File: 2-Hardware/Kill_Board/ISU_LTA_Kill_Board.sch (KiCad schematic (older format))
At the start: 31 parts, among them P1 CONN_01X02, P10 CONN_2, P12 CONN_2, P14 CONN_2, P16 CONN_2, P18 CONN_2, P2 CONN_01X02, P3 CONN_01X02, P4 CONN_01X03, P5 CONN_01X03, P6 CONN_01X03, P8 CONN_2, Q1 NMOS+PMOS, Q2 N-CH, Q3 N-CH, U1 ADAFRUIT_FEATHER, U2 LM2937

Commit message: Getting ready for fab
Unable to make board.  Footprint for Feather is lost, started working on new footprint but not complete yet.
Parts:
- removed R?: R_Shunt_US, symbol Device:R_Shunt_US
- C1, C2: footprint (none) -> Capacitors_SMD:C_0805_HandSoldering
- P1, P2, P3: footprint Connectors_Ian:CONN_2.54mm_1x2 -> Pin_Headers:Pin_Header_Angled_1x02_Pitch2.54mm
- P10: renamed from P14; footprint Connectors:DEANS_MICRO -> Connectors_JST:JST_VH_B2P-VH-B_2x3.96mm_Vertical
- P11: renamed from P16; footprint Connectors:DEANS_MICRO -> Connectors_JST:JST_VH_B2P-VH-B_2x3.96mm_Vertical
- P12: renamed from P18; footprint Connectors:DEANS_MICRO -> Connectors_JST:JST_VH_B2P-VH-B_2x3.96mm_Vertical
- P4, P5, P6: footprint Connectors_Ian:CONN_2.54mm_1x3 -> Pin_Headers:Pin_Header_Angled_1x03_Pitch2.54mm
- P7: renamed from P8; footprint Connectors:DEANS_MICRO -> Connectors_JST:JST_VH_B2P-VH-B_2x3.96mm_Vertical
- P8: renamed from P10; footprint Connectors:DEANS_MICRO -> Connectors_JST:JST_VH_B2P-VH-B_2x3.96mm_Vertical
- P9: renamed from P12; footprint Connectors:DEANS_MICRO -> Connectors_JST:JST_VH_B2P-VH-B_2x3.96mm_Vertical
- Q1: footprint SMD:SOT-23-6 -> TO_SOT_Packages_SMD:SOT-23-6
- R2: renamed from R1; footprint (none) -> Resistors_SMD:R_0805_HandSoldering
- R3: renamed from R2; footprint (none) -> Resistors_SMD:R_0805_HandSoldering
- R4: renamed from R3; footprint (none) -> Resistors_SMD:R_0805_HandSoldering
- R5: renamed from R4; footprint (none) -> Resistors_SMD:R_0805_HandSoldering
- R6: renamed from R5; footprint (none) -> Resistors_SMD:R_0805_HandSoldering
- R7: renamed from R6; footprint (none) -> Resistors_SMD:R_0805_HandSoldering
- R8: renamed from R7; footprint (none) -> Resistors_SMD:R_0805_HandSoldering
- R9: renamed from R8; footprint (none) -> Resistors_SMD:R_0805_HandSoldering
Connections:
- wire segments 118 -> 114
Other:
- moved on the sheet: P1

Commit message: Got correct footprint for feather, placed all parts on board
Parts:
- BT1: footprint Wire_Pads:SolderWirePad_2x_1-5mmDrill -> Connector_Wire:SolderWirePad_1x02_P7.62mm_Drill2.5mm
- D1: footprint LEDs:LED_0805 -> LED_SMD:LED_0805_2012Metric_Pad1.15x1.40mm_HandSolder
- Q1: footprint TO_SOT_Packages_SMD:SOT-23-6 -> Package_TO_SOT_SMD:SOT-23-6_Handsoldering
- Q2, Q3: footprint TO_SOT_Packages_SMD:SOT-404 -> Package_TO_SOT_SMD:TO-263-3_TabPin2
- S1: footprint Switches:DPDT_ESWITCH_EG2207 -> Button_Switch_THT:SW_CuK_JS202011CQN_DPDT_Straight
- U1: footprint Modules_Ian:ADAFRUIT_FEATHER -> Adafruit:AdafruitFeather
- U2: footprint TO_SOT_Packages_SMD:SOT-223 -> Package_TO_SOT_SMD:SOT-223
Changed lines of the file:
@@
 F 0 "Q1" H 5100 5090 60  0000 R CNN
 F 1 "NMOS+PMOS" H 5100 4720 60  0000 R CNN
-F 2 "TO_SOT_Packages_SMD:SOT-23-6" H 5100 4900 60  0001 C CNN
+F 2 "Package_TO_SOT_SMD:SOT-23-6_Handsoldering" H 5100 4900 60  0001 C CNN
 F 3 "" H 5100 4900 60  0001 C CNN
 F 4 "FDC6333CCT-ND" H 5100 4900 60  0001 C CNN "DigikeyNumber"
@@
 F 0 "Q1" H 5100 4490 60  0000 R CNN
 F 1 "NMOS+PMOS" H 5100 4120 60  0000 R CNN
-F 2 "TO_SOT_Packages_SMD:SOT-23-6" H 5100 4300 60  0001 C CNN
+F 2 "Package_TO_SOT_SMD:SOT-23-6_Handsoldering" H 5100 4300 60  0001 C CNN
 F 3 "" H 5100 4300 60  0001 C CNN
 F 4 "FDC6333CCT-ND" H 5100 4300 60  0001 C CNN "DigikeyNumber"
@@
 F 0 "Q2" H 6210 5270 60  0000 R CNN
 F 1 "N-CH" H 6210 4950 60  0000 R CNN
-F 2 "TO_SOT_Packages_SMD:SOT-404" H 6200 5100 60  0001 C CNN
+F 2 "Package_TO_SOT_SMD:TO-263-3_TabPin2" H 6200 5100 60  0001 C CNN
 F 3 "" H 6200 5100 60  0001 C CNN
 F 4 "568-6587-1-ND" H 6200 5100 60  0001 C CNN "DigikeyNumber"
@@
 F 0 "Q3" H 6210 6220 60  0000 R CNN
 F 1 "N-CH" H 6210 5900 60  0000 R CNN
-F 2 "TO_SOT_Packages_SMD:SOT-404" H 6200 6050 60  0001 C CNN
+F 2 "Package_TO_SOT_SMD:TO-263-3_TabPin2" H 6200 6050 60  0001 C CNN
 F 3 "" H 6200 6050 60  0001 C CNN
 F 4 "568-6587-1-ND" H 6200 6050 60  0001 C CNN "DigikeyNumber"
@@
 F 0 "U2" H 3700 4254 60  0000 C CNN
 F 1 "LM2937" H 3550 4650 60  0000 C CNN
-F 2 "TO_SOT_Packages_SMD:SOT-223" H 3550 4450 60  0001 C CNN
+F 2 "Package_TO_SOT_SMD:SOT-223" H 3550 4450 60  0001 C CNN
 F 3 "" H 3550 4450 60  0001 C CNN
 F 4 "LM2937IMP-3.3/NOPBCT-ND" H 3550 4450 60  0001 C CNN "DigikeyNumber"
@@
 F 0 "S1" H 5600 4750 60  0000 C CNN
 F 1 "DPDT" H 5500 5000 60  0000 C CNN
-F 2 "Switches:DPDT_ESWITCH_EG2207" H 5500 4850 60  0001 C CNN
+F 2 "Button_Switch_THT:SW_CuK_JS202011CQN_DPDT_Straight" H 5500 4850 60  0001 C CNN
 F 3 "" H 5500 4850 60  0001 C CNN
 F 4 "EG1940-ND" H 5500 4850 60  0001 C CNN "DigikeyNumber"
@@
 F 0 "S1" H 3600 3900 60  0000 C CNN
 F 1 "DPDT" H 3500 4150 60  0000 C CNN
-F 2 "Switches:DPDT_ESWITCH_EG2207" H 3500 4000 60  0001 C CNN
+F 2 "Button_Switch_THT:SW_CuK_JS202011CQN_DPDT_Straight" H 3500 4000 60  0001 C CNN
 F 3 "" H 3500 4000 60  0001 C CNN
 F 4 "EG1940-ND" H 3500 4000 60  0001 C CNN "DigikeyNumber"
@@
 F 0 "D1" H 7050 4750 50  0000 C CNN
 F 1 "LED" H 7050 4550 50  0000 C CNN
-F 2 "LEDs:LED_0805" H 7050 4650 60  0001 C CNN
+F 2 "LED_SMD:LED_0805_2012Metric_Pad1.15x1.40mm_HandSolder" H 7050 4650 60  0001 C CNN
 F 3 "" H 7050 4650 60  0001 C CNN
 F 4 "754-1141-1-ND" H 7050 4650 60  0001 C CNN "DigikeyNumber"
@@
 F 0 "BT1" H 2000 4800 50  0000 C CNN
 F 1 "BATTERY" H 2000 4410 50  0000 C CNN
-F 2 "Wire_Pads:SolderWirePad_2x_1-5mmDrill" H 2000 4600 60  0001 C CNN
+F 2 "Connector_Wire:SolderWirePad_1x02_P7.62mm_Drill2.5mm" H 2000 4600 60  0001 C CNN
 F 3 "" H 2000 4600 60  0001 C CNN
 	1    2000 4600
@@
 F 0 "U1" V 2350 1200 60  0000 C CNN
 F 1 "ADAFRUIT_FEATHER" V 2350 2000 60  0000 C CNN
-F 2 "Modules_Ian:ADAFRUIT_FEATHER" H 2300 1550 60  0001 C CNN
+F 2 "Adafruit:AdafruitFeather" H 2300 1550 60  0001 C CNN
 F 3 "" H 2300 1550 60  0000 C CNN
 	1    2150 1750
@@
 F 0 "U1" V 3450 1200 60  0000 C CNN
 F 1 "ADAFRUIT_FEATHER" V 3450 2000 60  0000 C CNN
-F 2 "Modules_Ian:ADAFRUIT_FEATHER" H 3400 1550 60  0001 C CNN
+F 2 "Adafruit:AdafruitFeather" H 3400 1550 60  0001 C CNN
 F 3 "" H 3400 1550 60  0000 C CNN
 	2    3250 1750

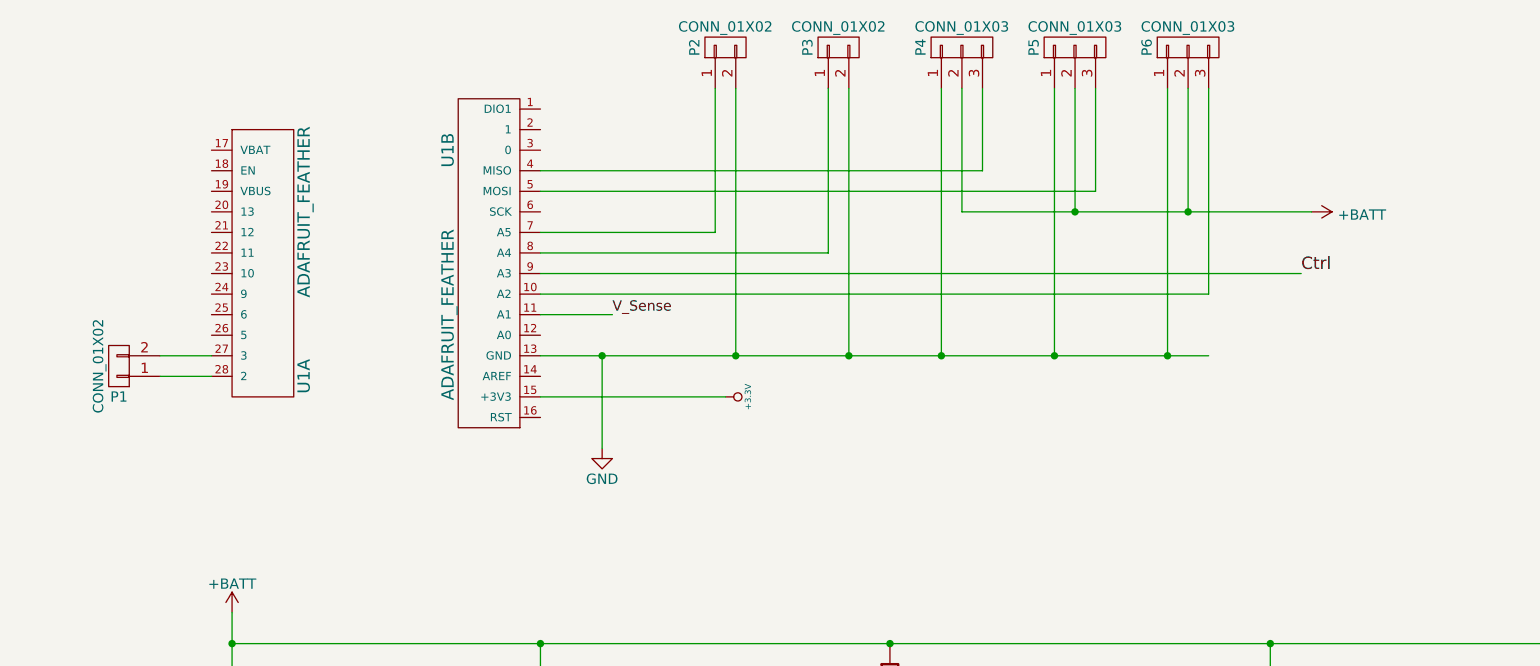
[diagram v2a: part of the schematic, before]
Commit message: Fixed pwm to have 3.3 v power and then added traces.
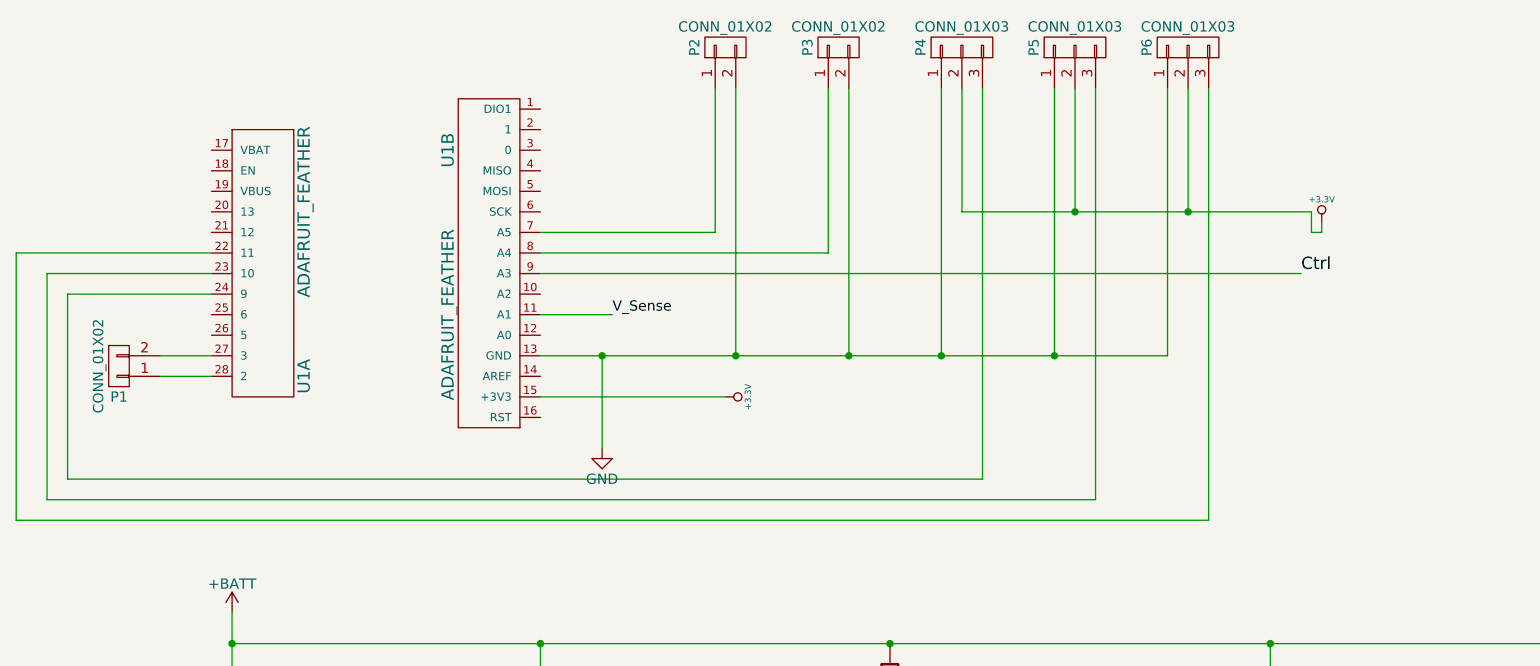
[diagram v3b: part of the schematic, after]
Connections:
- net +3.3V: now also P4.2 (P2), P5.2 (P2), P6.2 (P2)
- net +BATT: no longer P4.2 (P2), P5.2 (P2), P6.2 (P2)
- net at U1.22 (11): now also P6.3 (P3)
- net at U1.23 (10): now also P5.3 (P3)
- net at U1.24 (9): now also P4.3 (P3)
- net at U1.10 (A2): no longer P6.3 (P3)
- net at U1.4 (MISO): no longer P4.3 (P3)
- net at U1.5 (MOSI): no longer P5.3 (P3)
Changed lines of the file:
@@
 Wire Wire Line
 	6550 900  6550 2200
-Connection ~ 6550 2200
-Wire Wire Line
-	6550 2200 6750 2200
 Wire Wire Line
 	3500 2000 3850 2000
@@
 Wire Wire Line
 	6650 1500 7250 1500
+Wire Wire Line
+	2000 3600 3500 3600
+Wire Wire Line
+	1900 1700 950  1700
+Wire Wire Line
+	950  1700 950  3000
+Wire Wire Line
+	950  3000 6750 3000
+Wire Wire Line
+	6200 2900 1100 2900
+Wire Wire Line
+	1100 2900 1100 1800
+Wire Wire Line
+	1100 1800 1900 1800
+Wire Wire Line
+	6200 900  6200 2900
+Wire Wire Line
+	1900 1900 1200 1900
+Wire Wire Line
+	1200 1900 1200 2800
+Wire Wire Line
+	1200 2800 5650 2800
+Wire Wire Line
+	5650 900  5650 2800
+Wire Wire Line
+	6750 900  6750 3000
 $Comp
-L power:+BATT #PWR06
-U 1 1 5BDC1B50
-P 7250 1500
-F 0 "#PWR06" H 7250 1350 50  0001 C CNN
-F 1 "+BATT" V 7265 1628 50  0000 L CNN
-F 2 "" H 7250 1500 50  0001 C CNN
-F 3 "" H 7250 1500 50  0001 C CNN
-	1    7250 1500
-	0    1    1    0
+L ISU_LTA_Kill_Board-rescue:+3.3V-RESCUE-ISU_LTA_Kill_Board #PWR?
+U 1 1 5BDD1397
+P 7300 1550
+F 0 "#PWR?" H 7300 1510 30  0001 C CNN
+F 1 "+3.3V" H 7300 1660 30  0000 C CNN
+F 2 "" H 7300 1550 60  0001 C CNN
+F 3 "" H 7300 1550 60  0001 C CNN
+	1    7300 1550
+	1    0    0    -1
 $EndComp
 Wire Wire Line
-	5650 900  5650 1300
+	7250 1500 7250 1600
 Wire Wire Line
-	5650 1300 3500 1300
+	7250 1600 7300 1600
 Wire Wire Line
-	6200 900  6200 1400
-Wire Wire Line
-	6200 1400 3500 1400
-Wire Wire Line
-	6750 900  6750 1900
-Wire Wire Line
-	6750 1900 3500 1900
-Wire Wire Line
-	2000 3600 3500 3600
+	7300 1600 7300 1550
 $EndSCHEMATC

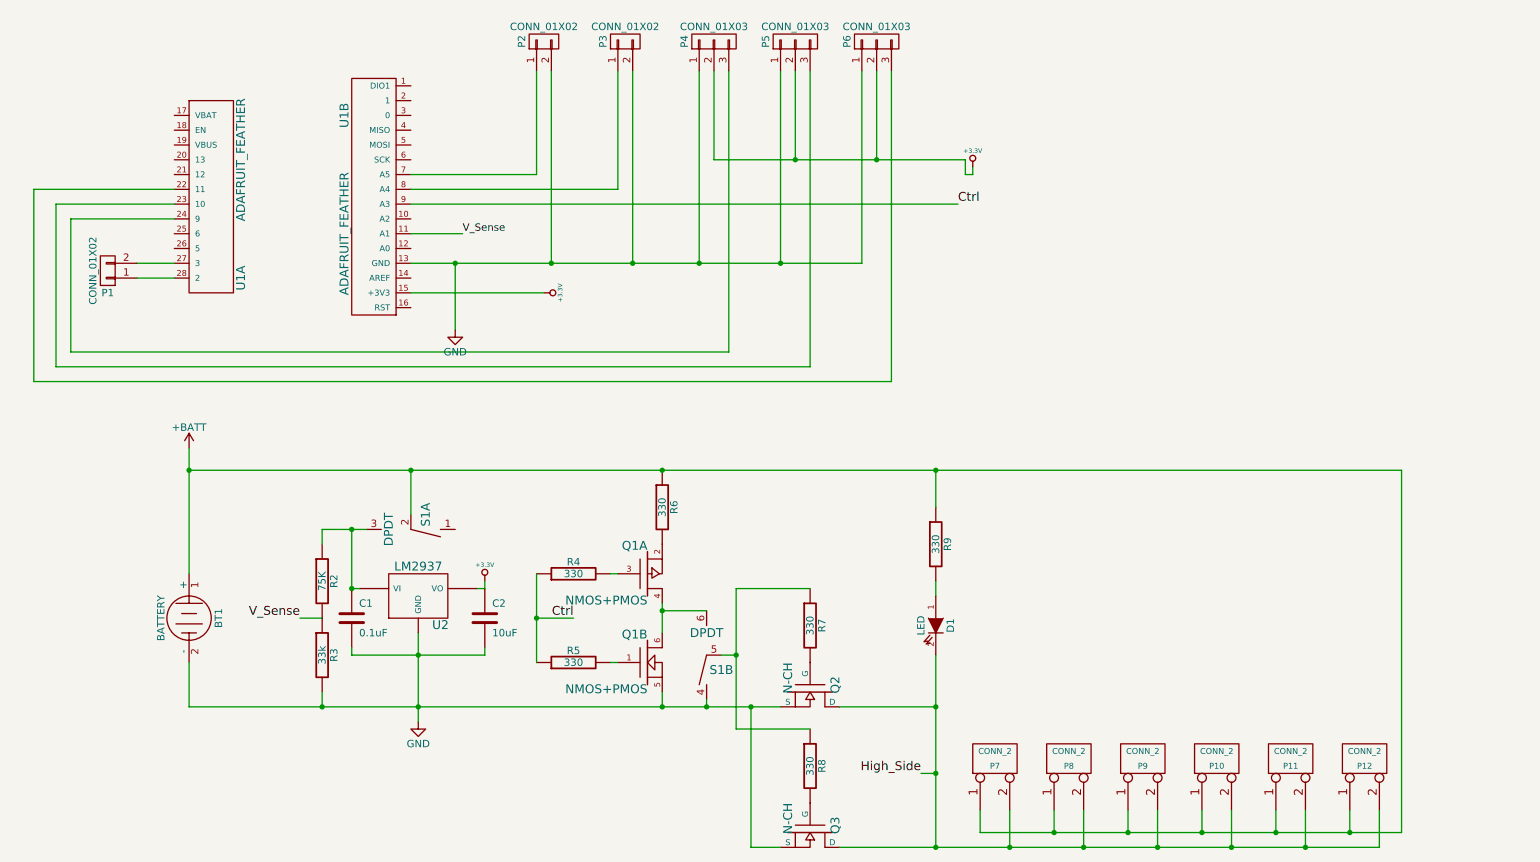
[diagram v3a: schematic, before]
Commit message: Update for bec add
Added 5v regulator and tied pwm power to them
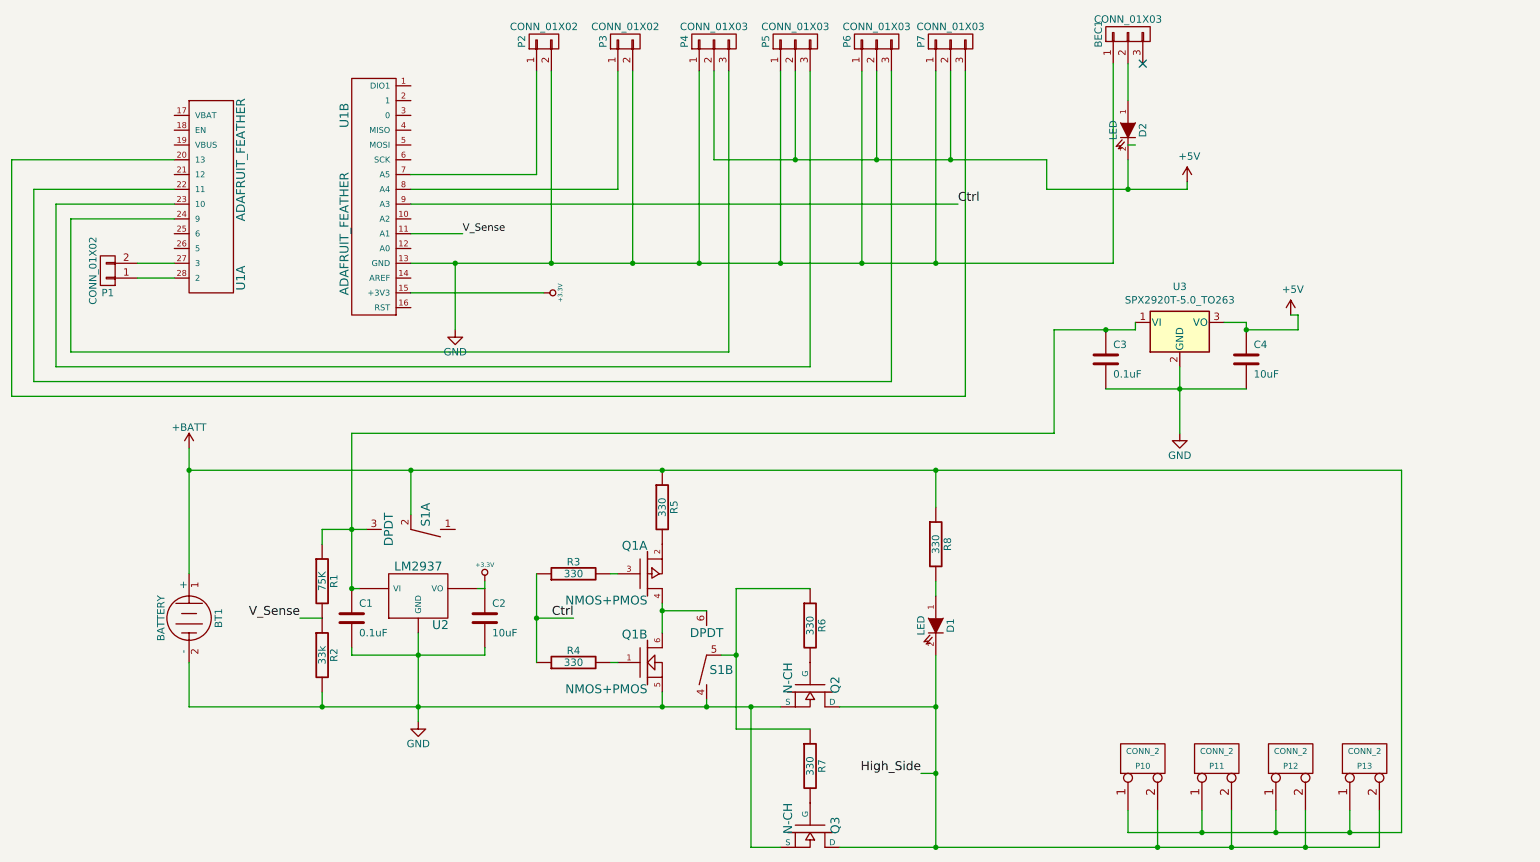
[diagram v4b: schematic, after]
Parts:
- removed P7, P8: CONN_2, Connectors_JST:JST_VH_B2P-VH-B_2x3.96mm_Vertical, symbol ISU_LTA_Kill_Board-rescue:CONN_2
- added BEC1, P7: CONN_01X03, Pin_Headers:Pin_Header_Angled_1x03_Pitch2.54mm, symbol ISU_LTA_Kill_Board-rescue:CONN_01X03
- added C3: 0.1uF, Capacitors_SMD:C_0805_HandSoldering, symbol ISU_LTA_Kill_Board-rescue:C-RESCUE-ISU_LTA_Kill_Board
- added C4: 10uF, Capacitors_SMD:C_0805_HandSoldering, symbol ISU_LTA_Kill_Board-rescue:C-RESCUE-ISU_LTA_Kill_Board
- added D2: LED, LEDs:LED_0805_HandSoldering, symbol ISU_LTA_Kill_Board-rescue:LED-RESCUE-ISU_LTA_Kill_Board
- added U3: SPX2920T-5.0_TO263, TO_SOT_Packages_SMD:TO-263-3_TabPin2, symbol Regulator_Linear:SPX2920T-5.0_TO263
- D1: footprint LED_SMD:LED_0805_2012Metric_Pad1.15x1.40mm_HandSolder -> LEDs:LED_0805_HandSoldering
- renumbered P9 to P10, P10 to P11, P11 to P12, P12 to P13, R2 to R1, R3 to R2, R4 to R3, R5 to R4, R6 to R5, R7 to R6, R8 to R7, R9 to R8
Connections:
- net +3.3V: no longer P4.2 (P2), P5.2 (P2), P6.2 (P2)
- net GND: now also BEC1.1 (P1), C3.2, C4.2, P7.1 (P1), U3.2 (GND)
- net at C1.1, R1.1, S1.3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: now also C3.1, U3.1 (VI)
- net at U1.20 (13): now also P7.3 (P3)
- new net: BEC1.2 (P2), D2.1 (A)
- new net +5V: C4.1, D2.2 (K), P4.2 (P2), P5.2 (P2), P6.2 (P2), P7.2 (P2), U3.3 (VO)
- no-connect marks 0 -> 1
